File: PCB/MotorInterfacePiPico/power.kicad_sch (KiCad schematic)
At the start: 15 parts, among them U2 OPA4197, U3 LM7810_TO220, U4 LM79L05_TO92

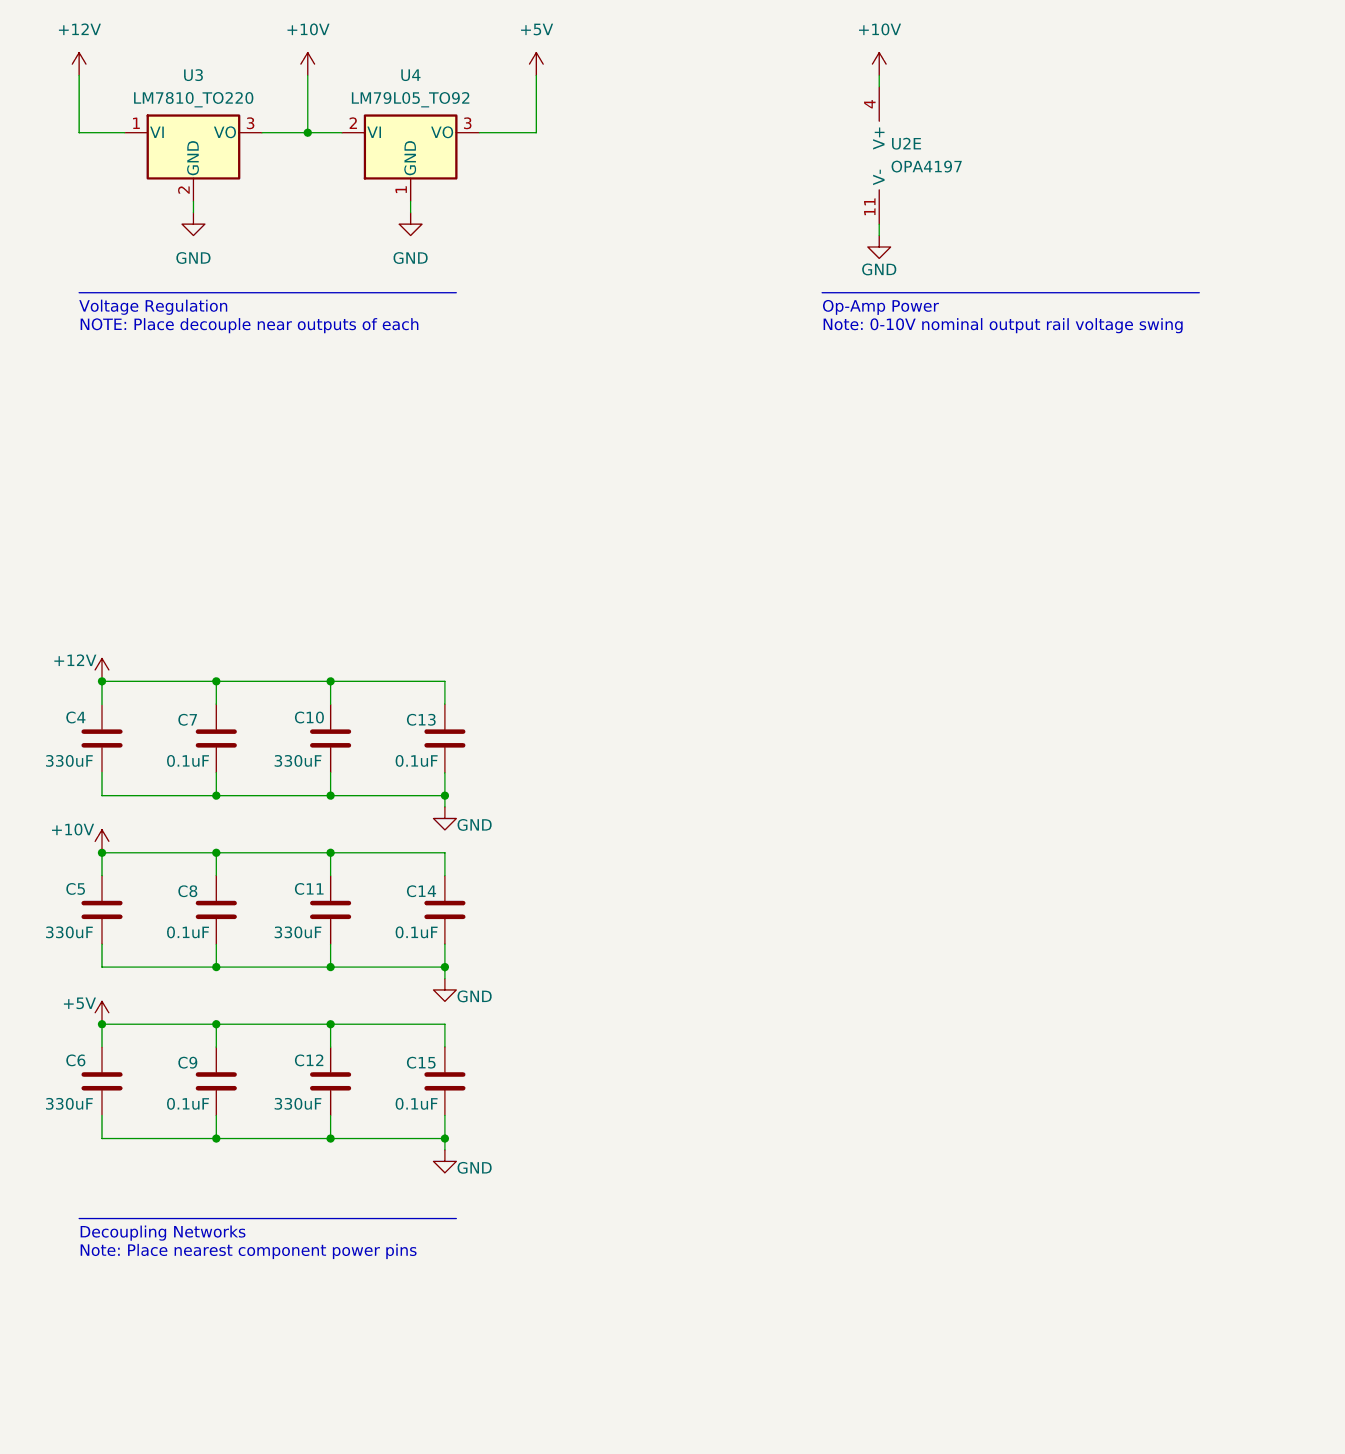
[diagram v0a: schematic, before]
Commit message: Layout complete, need silkscreen and BOM
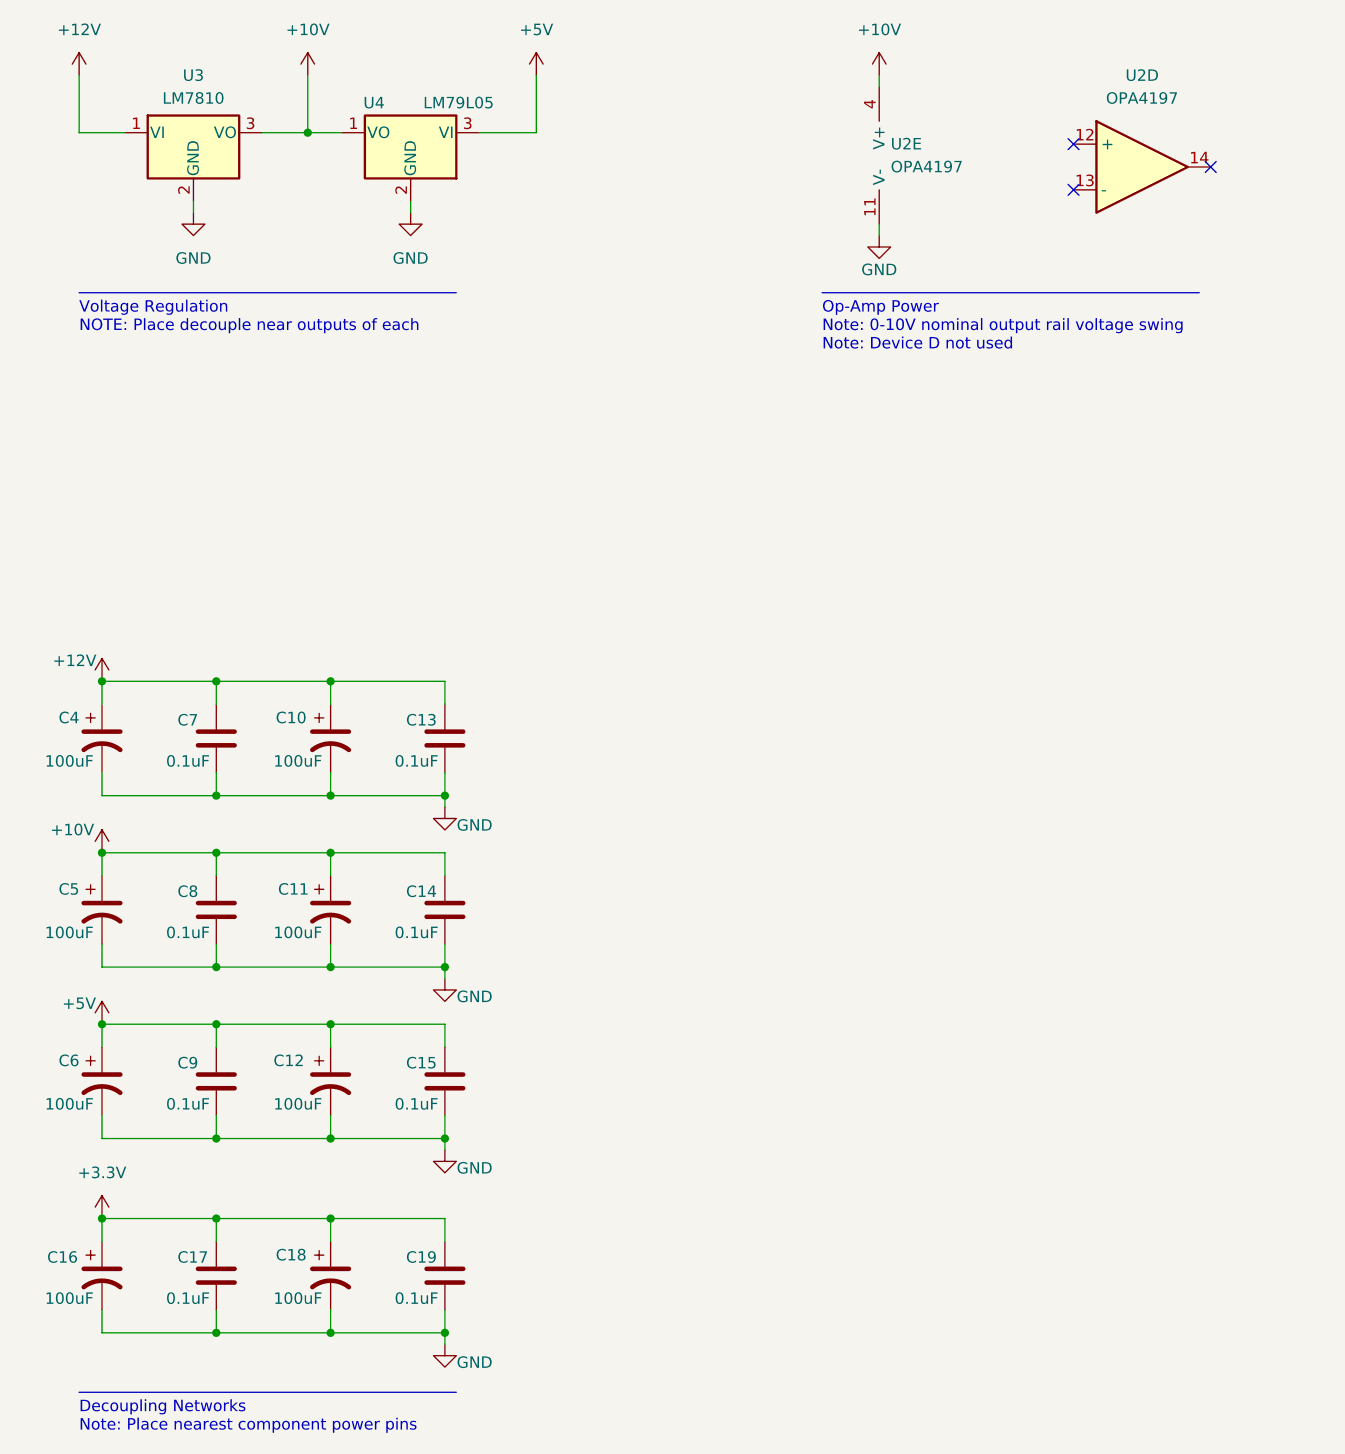
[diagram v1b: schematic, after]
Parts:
- added C16, C18: 100uF, TJR:C_Radial_D5.00mm_H12.5mm_P2.00mm, symbol TJR:C_Polarized_US
- added C17, C19: 0.1uF, TJR:C_Rect_L7.3mm_W2.5_H6.5mm_P5.0mm, symbol Device:C
- added unit 4 of U2
- C10, C11, C12, C4, C5, C6: value 330uF -> 100uF; footprint (none) -> TJR:C_Radial_D5.00mm_H12.5mm_P2.00mm; symbol Device:C -> TJR:C_Polarized_US; digikey (none) -> https://www.digikey.com/en/products/detail/rubycon/16ZLH100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
- C13, C14, C15, C8, C9: footprint (none) -> TJR:C_Rect_L7.3mm_W2.5_H6.5mm_P5.0mm
- C7: footprint (none) -> TJR:C_Rect_L7.3mm_W2.5_H6.5mm_P5.0mm; digikey (none) -> https://www.digikey.com/en/products/detail/epcos-tdk-electr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
- U2: footprint Package_SO:TSSOP-14_4.4x5mm_P0.65mm -> Package_SO:SOIC-14_3.9x8.7mm_P1.27mm
- U3: value LM7810_TO220 -> LM7810
- U4: value LM79L05_TO92 -> LM79L05; symbol Regulator_Linear:LM79L05_TO92 -> Regulator_Linear:LM78L05_TO92
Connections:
- net +10V: now also U4.1 (VO); no longer U4.2 (VI)
- net GND: now also U4.2 (GND), C16.2, C17.2, C18.2, C19.2; no longer U4.1 (GND)
- new net +3.3V: C16.1, C17.1, C18.1, C19.1
- no-connect marks 0 -> 3
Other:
- note added: "Op-Amp Power Note: 0-10V nominal output rail voltage swing Note: Device D not used"
- note removed: "Op-Amp Power Note: 0-10V nominal output rail voltage swing"

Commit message: Layout complete, need BOM
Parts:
- U2: footprint Package_SO:SOIC-14_3.9x8.7mm_P1.27mm -> TJR:D14_TEX
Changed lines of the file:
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@@
 			)
 		)
-		(property "Footprint" "Package_SO:SOIC-14_3.9x8.7mm_P1.27mm"
+		(property "Footprint" "TJR:D14_TEX"
 			(at 129.54 35.56 0)
 			(effects
@@
 			)
 		)
-		(property "Footprint" "Package_SO:SOIC-14_3.9x8.7mm_P1.27mm"
+		(property "Footprint" "TJR:D14_TEX"
 			(at 156.21 36.83 0)
 			(effects

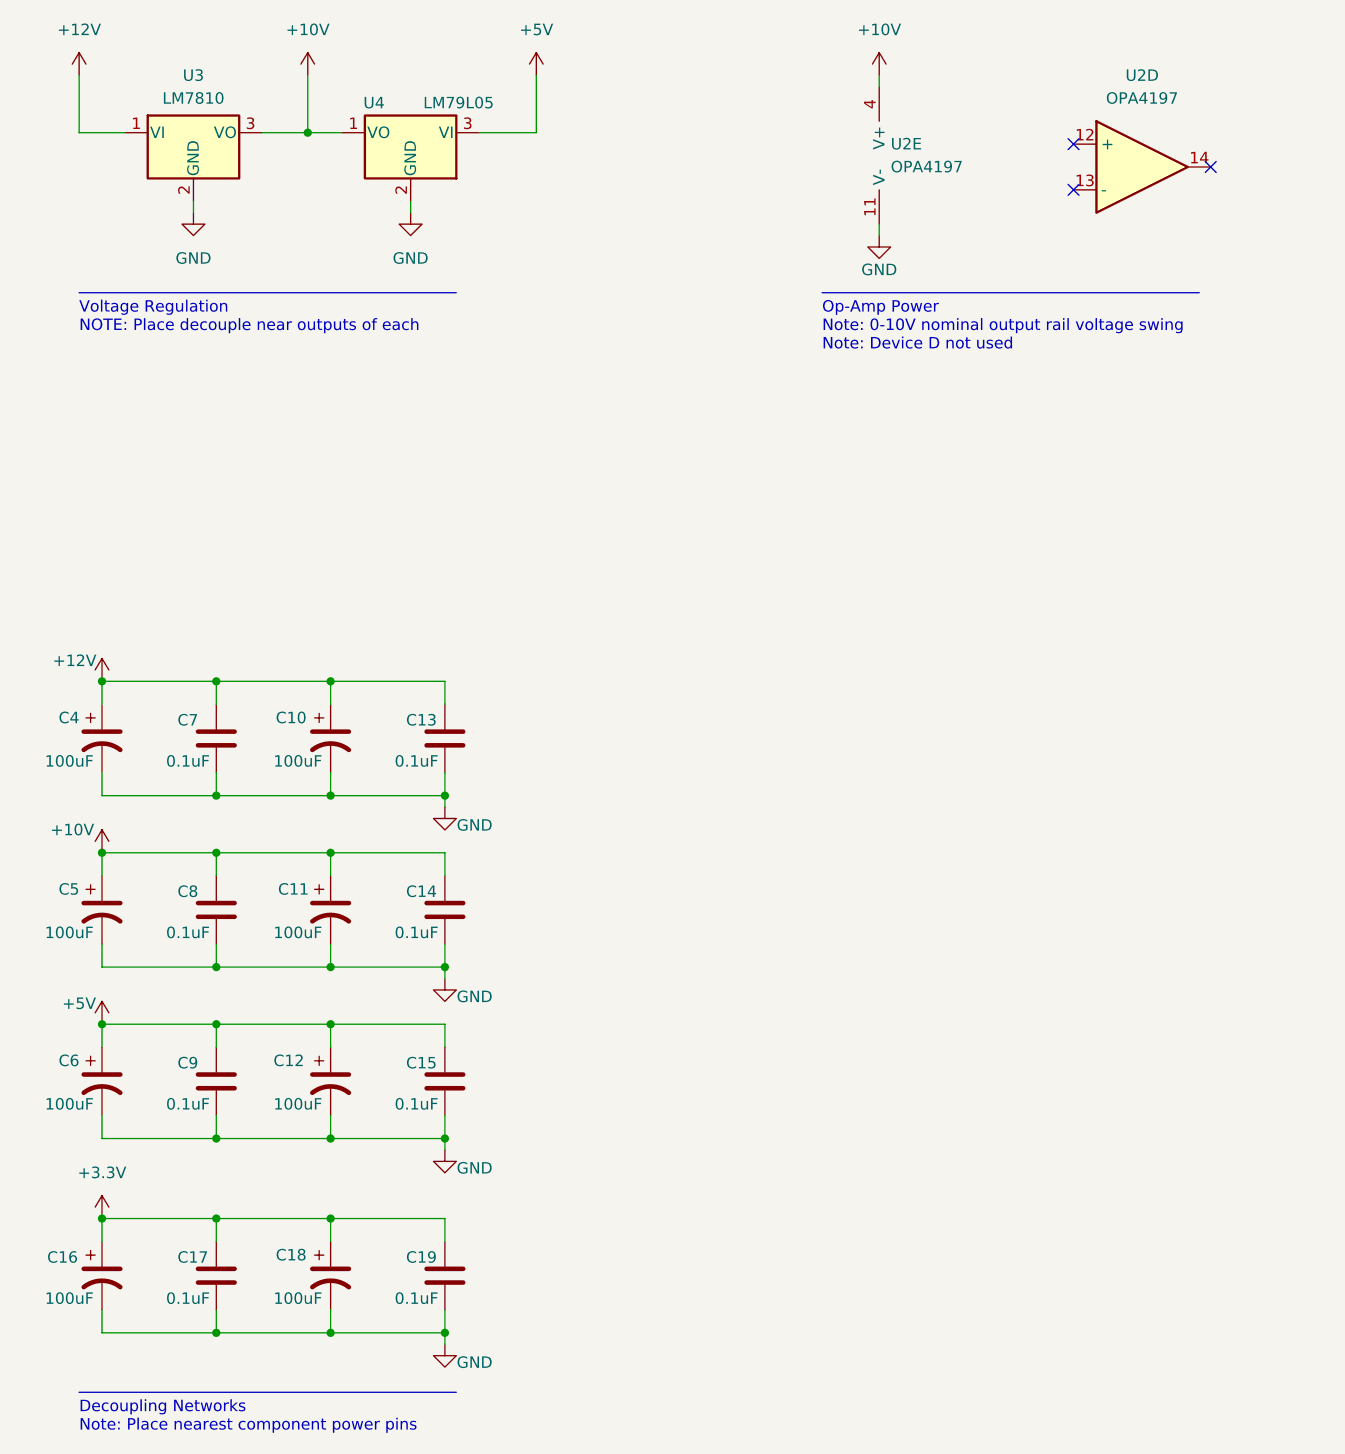
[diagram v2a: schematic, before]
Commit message: Surface Mount Board design
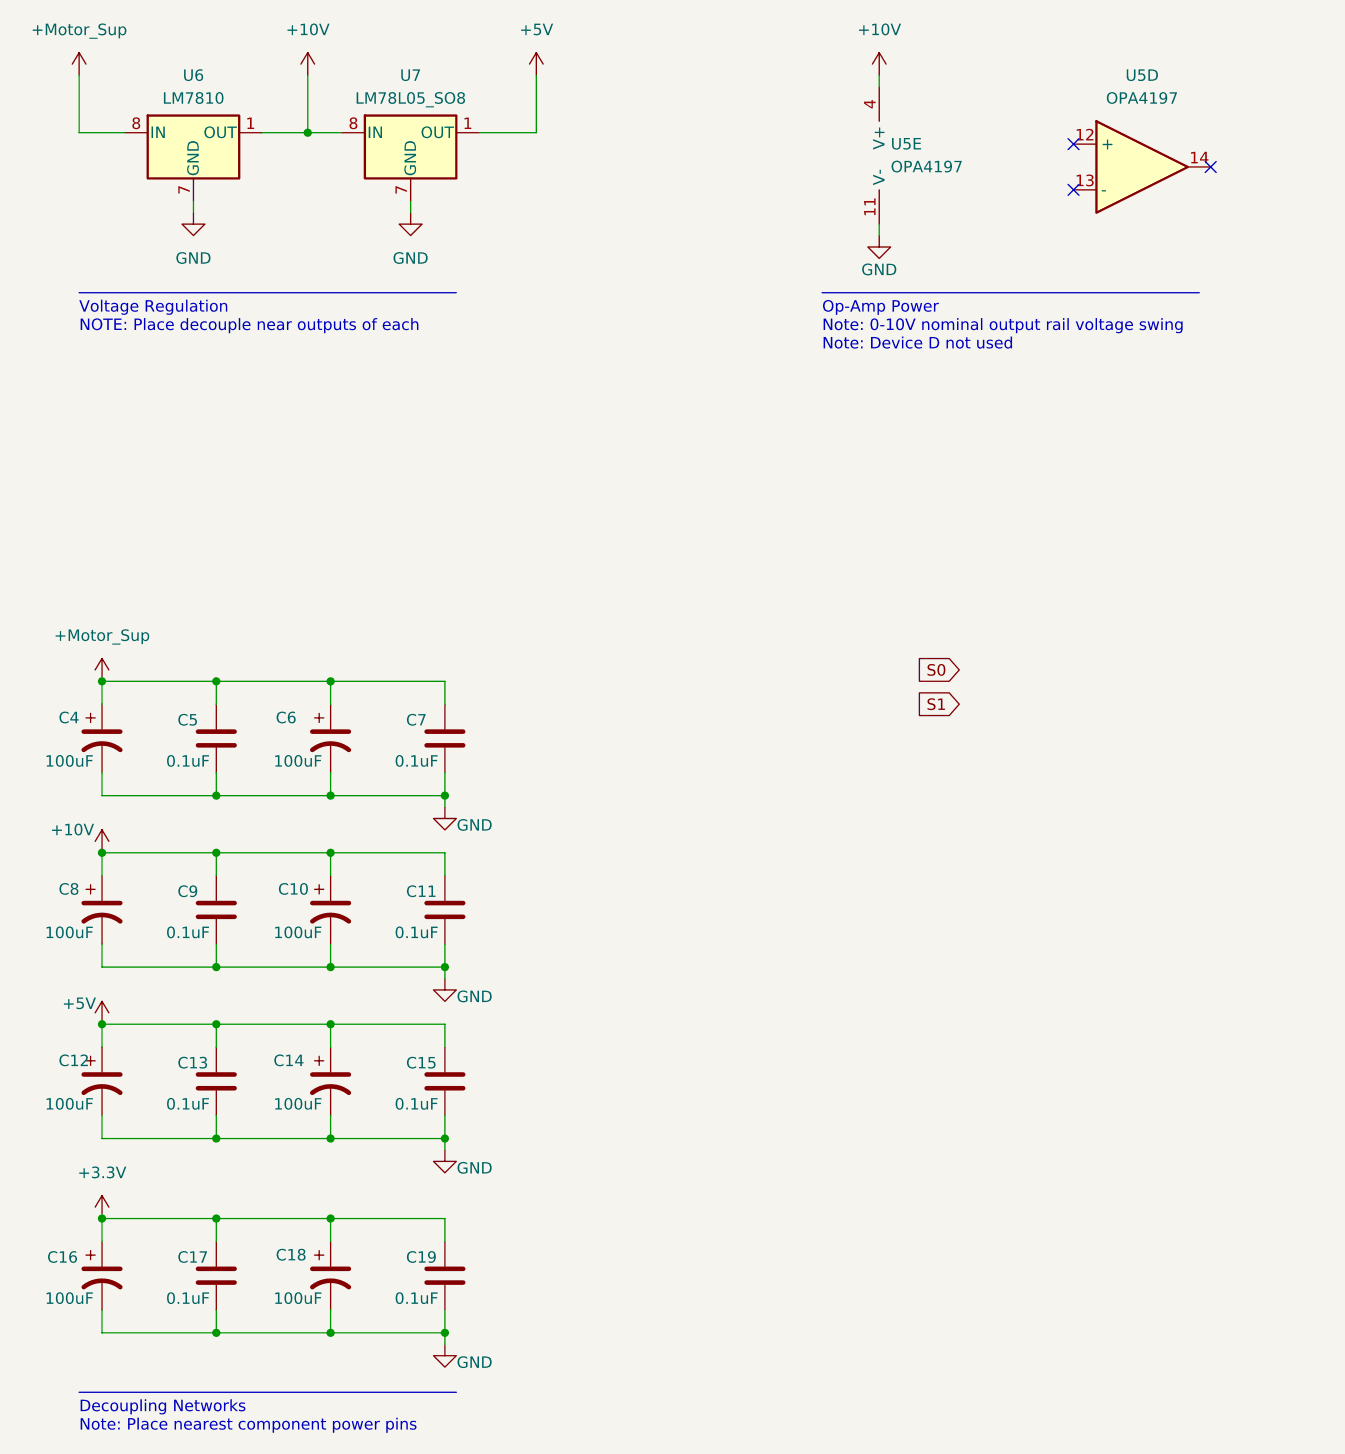
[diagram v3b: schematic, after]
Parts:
- removed U4: LM79L05, Package_TO_SOT_THT:TO-92_Inline, symbol Regulator_Linear:LM78L05_TO92
- added U7: LM78L05_SO8, Package_SO:SOIC-8_3.9x4.9mm_P1.27mm, symbol Regulator_Linear:LM78L05_SO8
- C10: renamed from C11; footprint TJR:C_Radial_D5.00mm_H12.5mm_P2.00mm -> Capacitor_Tantalum_SMD:CP_EIA-3216-10_Kemet-I
- C12: renamed from C6; footprint TJR:C_Radial_D5.00mm_H12.5mm_P2.00mm -> Capacitor_Tantalum_SMD:CP_EIA-3216-10_Kemet-I
- C14: renamed from C12; footprint TJR:C_Radial_D5.00mm_H12.5mm_P2.00mm -> Capacitor_Tantalum_SMD:CP_EIA-3216-10_Kemet-I
- C16, C18, C4: footprint TJR:C_Radial_D5.00mm_H12.5mm_P2.00mm -> Capacitor_Tantalum_SMD:CP_EIA-3216-10_Kemet-I
- C6: renamed from C10; footprint TJR:C_Radial_D5.00mm_H12.5mm_P2.00mm -> Capacitor_Tantalum_SMD:CP_EIA-3216-10_Kemet-I
- C8: renamed from C5; footprint TJR:C_Radial_D5.00mm_H12.5mm_P2.00mm -> Capacitor_Tantalum_SMD:CP_EIA-3216-10_Kemet-I
- C9: renamed from C8; footprint TJR:C_Rect_L7.3mm_W2.5_H6.5mm_P5.0mm -> Capacitor_SMD:C_0805_2012Metric
- U5: renamed from U2; footprint TJR:D14_TEX -> CustomBPA:SO-14_5.4_P1.27
- U6: renamed from U3; footprint Package_TO_SOT_THT:TO-220-3_Vertical -> Package_SO:SOIC-8_3.9x4.9mm_P1.27mm; symbol Regulator_Linear:LM7810_TO220 -> Regulator_Linear:L78L10_SO8
- renumbered C14 to C11, C9 to C13, C7 to C5, C13 to C7
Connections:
- net +10V: now also U6.1 (OUT), U7.8 (IN); no longer U6.3 (VO)
- net +5V: now also U7.1 (OUT)
- net GND: now also U6.3 (GND), U6.6 (GND), U6.7 (GND), U7.2 (GND), U7.3 (GND), U7.6 (GND), U7.7 (GND)
- net +12V renamed +Motor_Sup
- net +Motor_Sup: now also U6.8 (IN); no longer U6.1 (VI)
